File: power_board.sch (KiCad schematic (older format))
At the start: 40 parts, among them J1 RasPi_Conn2x20, J2 Power Supply, J3 MuddPi Conn, J4 LED Conn, Q1 Q_NMOS_DGS, Q10 Q_NMOS_DGS, Q11 Q_NMOS_DGS, Q12 Q_NMOS_DGS, Q13 Q_PMOS_DGS, Q14 Q_PMOS_DGS, Q15 Q_PMOS_DGS, Q16 Q_PMOS_DGS, Q17 Q_NMOS_DGS, Q18 Q_NMOS_DGS, Q19 Q_NMOS_DGS, Q2 Q_NMOS_DGS, Q20 Q_NMOS_DGS, Q21 Q_PMOS_DGS, Q22 Q_PMOS_DGS, Q23 Q_PMOS_DGS, Q24 Q_PMOS_DGS, Q3 Q_NMOS_DGS, Q4 Q_NMOS_DGS, Q5 Q_PMOS_DGS, Q6 Q_PMOS_DGS, Q7 Q_PMOS_DGS, Q8 Q_PMOS_DGS, Q9 Q_NMOS_DGS

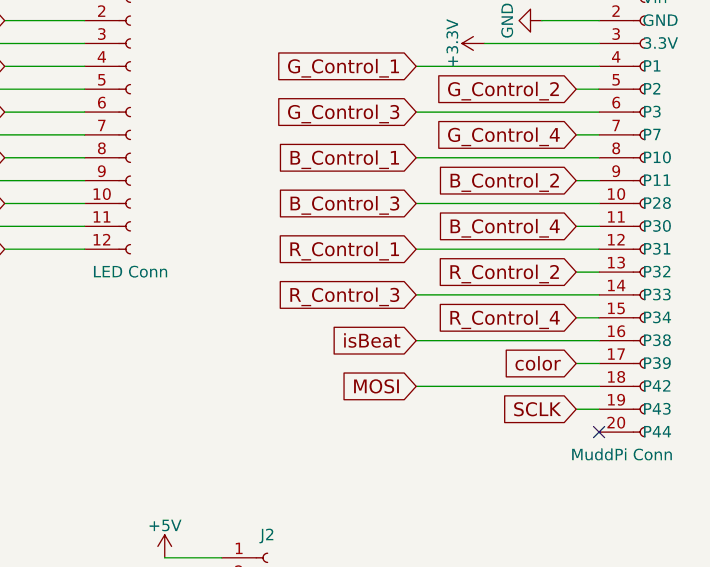
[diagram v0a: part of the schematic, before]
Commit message: Fixed some issues with the layout and made it conform to the OSH Park manufacturing specifications.  Ordered the board!!!
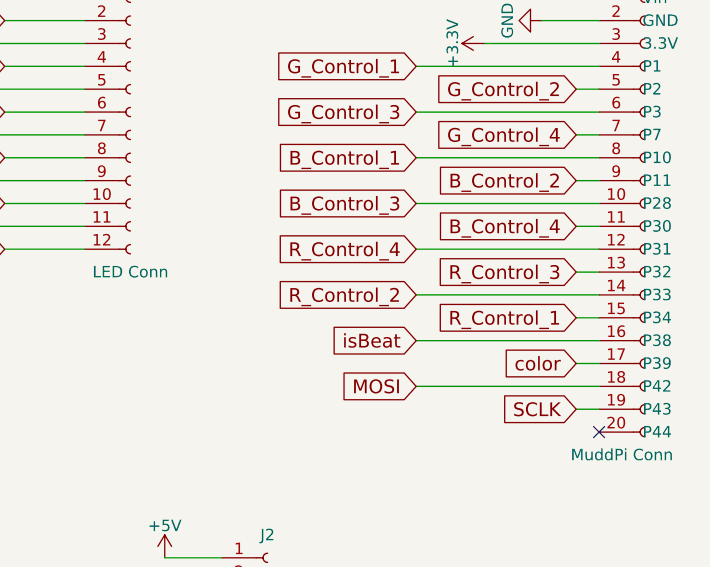
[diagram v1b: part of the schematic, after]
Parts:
- J2: footprint Connect:BARREL_JACK -> wall:BARREL_JACK
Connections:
- net R_Control_1: now also J3.15 (P34); no longer J3.12 (P31)
- net R_Control_2: now also J3.14 (P33); no longer J3.13 (P32)
- net R_Control_3: now also J3.13 (P32); no longer J3.14 (P33)
- net R_Control_4: now also J3.12 (P31); no longer J3.15 (P34)
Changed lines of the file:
@@
 	10200 1000 10700 1000
 Text GLabel 9900 1900 0    60   Input ~ 0
-R_Control_1
+R_Control_4
 Text GLabel 9900 1100 0    60   Input ~ 0
 G_Control_1
@@
 B_Control_1
 Text GLabel 10600 2000 0    60   Input ~ 0
-R_Control_2
+R_Control_3
 Text GLabel 10600 1200 0    60   Input ~ 0
 G_Control_2
@@
 B_Control_2
 Text GLabel 9900 2100 0    60   Input ~ 0
-R_Control_3
+R_Control_2
 Text GLabel 9900 1300 0    60   Input ~ 0
 G_Control_3
@@
 B_Control_3
 Text GLabel 10600 2200 0    60   Input ~ 0
-R_Control_4
+R_Control_1
 Text GLabel 10600 1400 0    60   Input ~ 0
 G_Control_4
@@
 F 0 "J2" H 9250 3550 50  0000 C CNN
 F 1 "Power Supply" H 9250 3150 50  0000 C CNN
-F 2 "Connect:BARREL_JACK" H 9250 3350 50  0001 C CNN
+F 2 "wall:BARREL_JACK" H 9250 3350 50  0001 C CNN
 F 3 "" H 9250 3350 50  0001 C CNN
 	1    9250 3350
